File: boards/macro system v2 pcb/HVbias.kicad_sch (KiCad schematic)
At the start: 7 parts, among them J11 Conn_01x03, U8 ADA4097

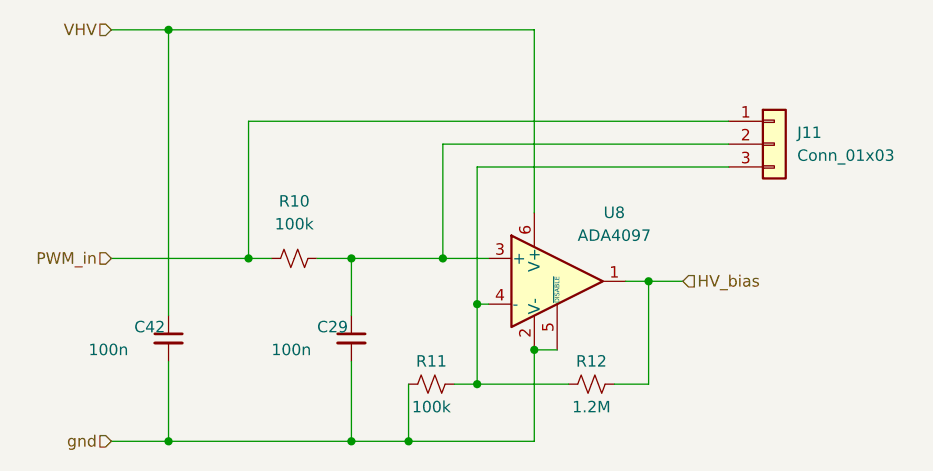
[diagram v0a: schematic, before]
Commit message: create new LD only mount PCB
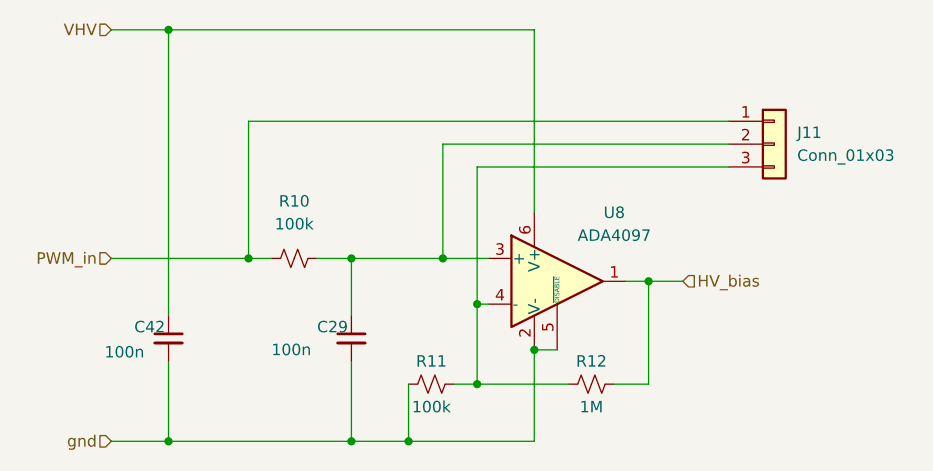
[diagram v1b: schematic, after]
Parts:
- R12: value 1.2M -> 1M
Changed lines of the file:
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@@
 		)
 		(property "Value" "100n"
-			(at 93.98 104.14 0)
+			(at 95.758 104.394 0)
 			(effects
 				(font
@@
 			)
 		)
-		(property "Value" "1.2M"
+		(property "Value" "1M"
 			(at 149.86 110.49 90)
 			(effects
